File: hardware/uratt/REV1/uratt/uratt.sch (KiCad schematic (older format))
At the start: 65 parts, among them J1 USB_B_Micro, J2 Micro_SD_Card, J3 Conn_01x10, J4 Conn_01x04, J5 Conn_01x04, Q1 MMBT3904, Q2 MMBT3904, SW1 SW_Push, SW2 SW_Push, U1 SN65220DBVR, U2 CP2102N-A02-GQFN24, U3 ESP32-WROOM-32E

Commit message: work in progress on REV1 schematic/PCB
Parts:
- added R56: 22.1K, Resistor_SMD:R_0603_1608Metric, symbol Device:R_Small_US
- added R57: 47.5K, Resistor_SMD:R_0603_1608Metric, symbol Device:R_Small_US
- added R58: 1K, Resistor_SMD:R_0603_1608Metric, symbol Device:R_Small_US
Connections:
- net +3.3VSW: now also R58.2
- net +5VUSB: now also R56.2; no longer U2.8 (VBUS)
- net ALARM_SCL: now also D5.3
- net DTR: now also R18.2
- net EXP_SDA: now also D4.3
- net GND: now also R57.1; no longer R18.1
- net SD_DAT0: now also R18.1; no longer R18.2
- net at U2.9 (~RSTb): now also R58.1
- net at J5.1 (Pin_1), R24.1: no longer D5.3
- net at J5.2 (Pin_2), R20.1: no longer D4.3
- new net: R56.1, R57.2, U2.8 (VBUS)
- no-connect marks 19 -> 18
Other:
- note added: "USE DTR FROM \nUSB-SERIAL FOR\nSTRAPPING OF IO2\nDURING PROGRAMMING\n(FOR SD CARD PULLUPS)"
- moved on the sheet: C1, C2, D5, R18

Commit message: uratt REV1 work, remove front panel, place new parts, partial routing
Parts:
- J3: footprint Connector_FFC-FPC:TE_1-1734839-0_1x10-1MP_P0.5mm_Horizontal -> uratt:TE_1-1734742-0
- renumbered D4 to D2, D2 to D3, D3 to D4, FB3 to FB2, FB2 to FB3, R56 to R10, R57 to R11, R58 to R12, R10 to R13, R11 to R14, R12 to R15, R13 to R16, R14 to R17, R15 to R18, R16 to R19, R17 to R20, R18 to R21, R54 to R22, R55 to R23, R20 to R24, R19 to R25, R24 to R26, R21 to R27, R22 to R28, R23 to R29, R25 to R30
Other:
- note added: "FRONT PANEL PCB\nSEPARATE PROJECT"
- note removed: "FRONT PANEL"

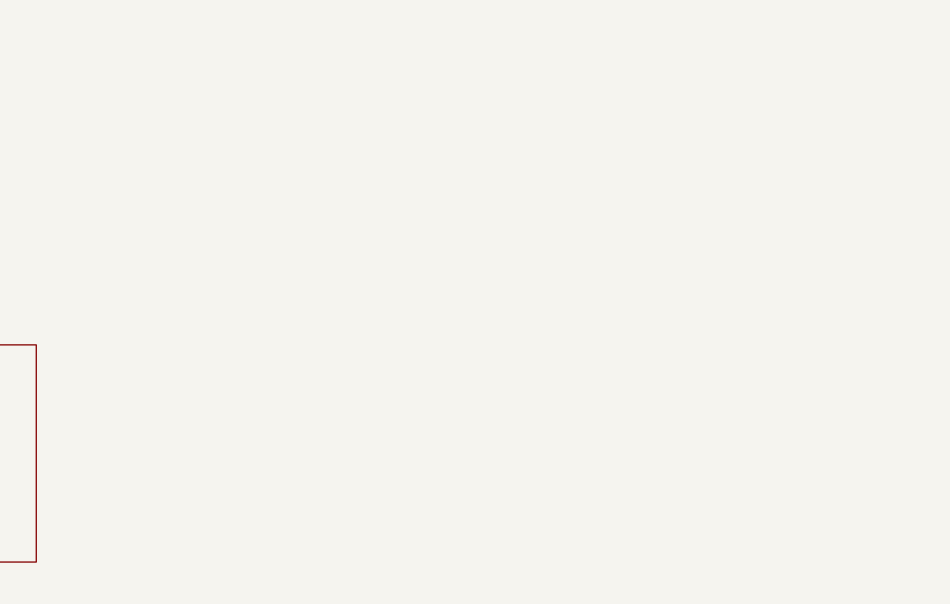
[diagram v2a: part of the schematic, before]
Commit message: add breakaway rails & fiducials for assembly
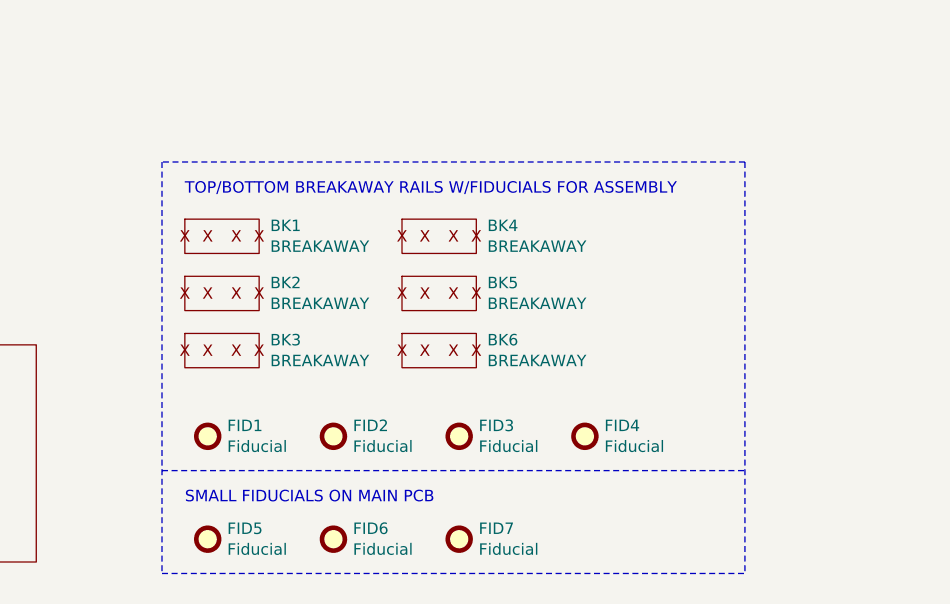
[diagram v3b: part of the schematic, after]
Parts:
- added BK1, BK2, BK3, BK4, BK5, BK6: BREAKAWAY, uratt:RATT_BITE, symbol uratt:BREAKAWAY
- added FID1, FID2, FID3, FID4: Fiducial, Fiducial:Fiducial_1mm_Mask3mm, symbol Mechanical:Fiducial
- added FID5, FID6, FID7: Fiducial, Fiducial:Fiducial_0.75mm_Mask1.5mm, symbol Mechanical:Fiducial
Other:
- note added: "SMALL FIDUCIALS ON MAIN PCB\n"
- note added: "TOP/BOTTOM BREAKAWAY RAILS W/FIDUCIALS FOR ASSEMBLY"
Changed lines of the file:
@@
 Wire Wire Line
 	13600 4900 13700 4900
+$Comp
+L uratt:BREAKAWAY BK1
+U 1 1 60010A6C
+P 3150 8600
+F 0 "BK1" H 3523 8571 50  0000 L CNN
+F 1 "BREAKAWAY" H 3523 8480 50  0000 L CNN
+F 2 "uratt:RATT_BITE" H 3150 8600 50  0001 C CNN
+F 3 "" H 3150 8600 50  0001 C CNN
+	1    3150 8600
+	1    0    0    -1
+$EndComp
+$Comp
+L uratt:BREAKAWAY BK2
+U 1 1 60012D43
+P 3150 8850
+F 0 "BK2" H 3523 8821 50  0000 L CNN
+F 1 "BREAKAWAY" H 3523 8730 50  0000 L CNN
+F 2 "uratt:RATT_BITE" H 3150 8850 50  0001 C CNN
+F 3 "" H 3150 8850 50  0001 C CNN
+	1    3150 8850
+	1    0    0    -1
+$EndComp
+$Comp
+L uratt:BREAKAWAY BK3
+U 1 1 60027317
+P 3150 9100
+F 0 "BK3" H 3523 9071 50  0000 L CNN
+F 1 "BREAKAWAY" H 3523 8980 50  0000 L CNN
+F 2 "uratt:RATT_BITE" H 3150 9100 50  0001 C CNN
+F 3 "" H 3150 9100 50  0001 C CNN
+	1    3150 9100
+	1    0    0    -1
+$EndComp
+$Comp
+L uratt:BREAKAWAY BK4
+U 1 1 6003BB66
+P 4100 8600
+F 0 "BK4" H 4473 8571 50  0000 L CNN
+F 1 "BREAKAWAY" H 4473 8480 50  0000 L CNN
+F 2 "uratt:RATT_BITE" H 4100 8600 50  0001 C CNN
+F 3 "" H 4100 8600 50  0001 C CNN
+	1    4100 8600
+	1    0    0    -1
+$EndComp
+$Comp
+L uratt:BREAKAWAY BK5
+U 1 1 600502D6
+P 4100 8850
+F 0 "BK5" H 4473 8821 50  0000 L CNN
+F 1 "BREAKAWAY" H 4473 8730 50  0000 L CNN
+F 2 "uratt:RATT_BITE" H 4100 8850 50  0001 C CNN
+F 3 "" H 4100 8850 50  0001 C CNN
+	1    4100 8850
+	1    0    0    -1
+$EndComp
+$Comp
+L uratt:BREAKAWAY BK6
+U 1 1 600648B2
+P 4100 9100
+F 0 "BK6" H 4473 9071 50  0000 L CNN
+F 1 "BREAKAWAY" H 4473 8980 50  0000 L CNN
+F 2 "uratt:RATT_BITE" H 4100 9100 50  0001 C CNN
+F 3 "" H 4100 9100 50  0001 C CNN
+	1    4100 9100
+	1    0    0    -1
+$EndComp
+$Comp
+L Mechanical:Fiducial FID1
+U 1 1 60092BA0
+P 3250 9550
+F 0 "FID1" H 3335 9596 50  0000 L CNN
+F 1 "Fiducial" H 3335 9505 50  0000 L CNN
+F 2 "Fiducial:Fiducial_1mm_Mask3mm" H 3250 9550 50  0001 C CNN
+F 3 "~" H 3250 9550 50  0001 C CNN
+	1    3250 9550
+	1    0    0    -1
+$EndComp
+$Comp
+L Mechanical:Fiducial FID2
+U 1 1 60093902
+P 3800 9550
+F 0 "FID2" H 3885 9596 50  0000 L CNN
+F 1 "Fiducial" H 3885 9505 50  0000 L CNN
+F 2 "Fiducial:Fiducial_1mm_Mask3mm" H 3800 9550 50  0001 C CNN
+F 3 "~" H 3800 9550 50  0001 C CNN
+	1    3800 9550
+	1    0    0    -1
+$EndComp
+$Comp
+L Mechanical:Fiducial FID3
+U 1 1 600A8044
+P 4350 9550
+F 0 "FID3" H 4435 9596 50  0000 L CNN
+F 1 "Fiducial" H 4435 9505 50  0000 L CNN
+F 2 "Fiducial:Fiducial_1mm_Mask3mm" H 4350 9550 50  0001 C CNN
+F 3 "~" H 4350 9550 50  0001 C CNN
+	1    4350 9550
+	1    0    0    -1
+$EndComp
+$Comp
+L Mechanical:Fiducial FID4
+U 1 1 600BC69E
+P 4900 9550
+F 0 "FID4" H 4985 9596 50  0000 L CNN
+F 1 "Fiducial" H 4985 9505 50  0000 L CNN
+F 2 "Fiducial:Fiducial_1mm_Mask3mm" H 4900 9550 50  0001 C CNN
+F 3 "~" H 4900 9550 50  0001 C CNN
+	1    4900 9550
+	1    0    0    -1
+$EndComp
+$Comp
+L Mechanical:Fiducial FID5
+U 1 1 60131A17
+P 3250 10000
+F 0 "FID5" H 3335 10046 50  0000 L CNN
+F 1 "Fiducial" H 3335 9955 50  0000 L CNN
+F 2 "Fiducial:Fiducial_0.75mm_Mask1.5mm" H 3250 10000 50  0001 C CNN
+F 3 "~" H 3250 10000 50  0001 C CNN
+	1    3250 10000
+	1    0    0    -1
+$EndComp
+$Comp
+L Mechanical:Fiducial FID6
+U 1 1 601460D2
+P 3800 10000
+F 0 "FID6" H 3885 10046 50  0000 L CNN
+F 1 "Fiducial" H 3885 9955 50  0000 L CNN
+F 2 "Fiducial:Fiducial_0.75mm_Mask1.5mm" H 3800 10000 50  0001 C CNN
+F 3 "~" H 3800 10000 50  0001 C CNN
+	1    3800 10000
+	1    0    0    -1
+$EndComp
+$Comp
+L Mechanical:Fiducial FID7
+U 1 1 601AD5D9
+P 4350 10000
+F 0 "FID7" H 4435 10046 50  0000 L CNN
+F 1 "Fiducial" H 4435 9955 50  0000 L CNN
+F 2 "Fiducial:Fiducial_0.75mm_Mask1.5mm" H 4350 10000 50  0001 C CNN
+F 3 "~" H 4350 10000 50  0001 C CNN
+	1    4350 10000
+	1    0    0    -1
+$EndComp
+Text Notes 3150 8500 0    50   ~ 0
+TOP/BOTTOM BREAKAWAY RAILS W/FIDUCIALS FOR ASSEMBLY
+Wire Notes Line
+	3050 9700 5600 9700
+Wire Notes Line
+	5600 8350 3050 8350
+Text Notes 3150 9850 0    50   ~ 0
+SMALL FIDUCIALS ON MAIN PCB\n
+Wire Notes Line
+	3050 10150 5600 10150
+Wire Notes Line
+	5600 8350 5600 10150
+Wire Notes Line
+	3050 8350 3050 10150
 $EndSCHEMATC

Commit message: uratt REV1 change inductor, cleanups, add 3.3V motor option, silk work, 12 pin FFC
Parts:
- J3: footprint uratt:TE_1-1734742-0 -> uratt:TE_1-1734742-2; symbol Connector_Generic:Conn_01x10 -> Connector_Generic:Conn_01x12; Alt MFR Part ZF5S-10-01-T-WT-TR -> (none); Digikey A100293CT-ND -> 1-1734742-2
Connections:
- net +3.3VSW: now also J3.2 (Pin_2)
- net BEEPER: now also J3.9 (Pin_9); no longer J3.8 (Pin_8)
- net FP_TOUCH_BTN: now also J3.10 (Pin_10); no longer J3.9 (Pin_9)
- net GND: now also J3.11 (Pin_11), J3.12 (Pin_12); no longer J3.10 (Pin_10)
- net LCD_BL: now also J3.3 (Pin_3); no longer J3.2 (Pin_2)
- net LCD_CLK: now also J3.7 (Pin_7); no longer J3.6 (Pin_6)
- net LCD_CS: now also J3.4 (Pin_4); no longer J3.3 (Pin_3)
- net LCD_DC: now also J3.6 (Pin_6); no longer J3.5 (Pin_5)
- net LCD_MOSI: now also J3.8 (Pin_8); no longer J3.7 (Pin_7)
- net LCD_RESET: now also J3.5 (Pin_5); no longer J3.4 (Pin_4)
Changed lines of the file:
@@
-	1    0    0    -1
-$EndComp
-$Comp
-L Connector_Generic:Conn_01x10 J3
-U 1 1 62A9ED39
-P 14300 1600
-F 0 "J3" H 14300 2100 50  0000 C CNN
-F 1 "Conn_01x10" H 14450 950 50  0000 C CNN
-F 2 "uratt:TE_1-1734742-0" H 14300 1600 50  0001 C CNN
-F 3 "https://www.te.com/commerce/DocumentDelivery/DDEController?Action=srchrtrv&DocNm=1734839&DocType=Customer+Drawing&DocLang=English" H 14300 1600 50  0001 C CNN
-F 4 "A100293CT-ND" H 14300 1600 50  0001 C CNN "Digikey"
-F 5 "ZF5S-10-01-T-WT-TR" H 14300 1600 50  0001 C CNN "Alt MFR Part"
-	1    14300 1600
 	1    0    0    -1
 $EndComp
@@
 LCD_CLK
 Wire Wire Line
-	14100 1200 12750 1200
+	14100 1200 14000 1200
 Wire Wire Line
 	12750 1200 12750 1000
@@
 L power:GND #PWR031
 U 1 1 62DCEE0A
-P 14000 2200
-F 0 "#PWR031" H 14000 1950 50  0001 C CNN
-F 1 "GND" H 14005 2027 50  0000 C CNN
-F 2 "" H 14000 2200 50  0001 C CNN
-F 3 "" H 14000 2200 50  0001 C CNN
-	1    14000 2200
+P 14000 2300
+F 0 "#PWR031" H 14000 2050 50  0001 C CNN
+F 1 "GND" H 14005 2127 50  0000 C CNN
+F 2 "" H 14000 2300 50  0001 C CNN
+F 3 "" H 14000 2300 50  0001 C CNN
+	1    14000 2300
 	1    0    0    -1
 $EndComp
@@
 BEEPER
 Wire Wire Line
-	14000 2200 14000 2100
+	14000 2300 14000 2200
 Wire Wire Line
 	14000 2100 14100 2100
@@
 Wire Notes Line
 	3050 8350 3050 10150
+$Comp
+L Connector_Generic:Conn_01x12 J3
+U 1 1 62A9ED39
+P 14300 1600
+F 0 "J3" H 14300 2200 50  0000 C CNN
+F 1 "Conn_01x10" H 14450 900 50  0000 C CNN
+F 2 "uratt:TE_1-1734742-2" H 14300 1600 50  0001 C CNN
+F 3 "https://www.te.com/commerce/DocumentDelivery/DDEController?Action=srchrtrv&DocNm=1734839&DocType=Customer+Drawing&DocLang=English" H 14300 1600 50  0001 C CNN
+F 4 "1-1734742-2" H 14300 1600 50  0001 C CNN "Digikey"
+F 5 "" H 14300 1600 50  0001 C CNN "Alt MFR Part"
+	1    14300 1600
+	1    0    0    -1
+$EndComp
+Wire Wire Line
+	14100 2200 14000 2200
+Connection ~ 14000 2200
+Wire Wire Line
+	14000 2200 14000 2100
+Wire Wire Line
+	14100 1100 14000 1100
+Wire Wire Line
+	14000 1100 14000 1200
+Connection ~ 14000 1200
+Wire Wire Line
+	14000 1200 12750 1200
 $EndSCHEMATC
